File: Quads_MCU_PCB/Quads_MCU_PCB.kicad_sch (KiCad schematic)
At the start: 74 parts, among them J1 USB_C_Receptacle_USB2.0_16P, J2 Conn_01x06_Pin, J3 Conn_01x02_Pin, SW1 SW_Push, U1 STM32H723ZGTx, U2 TCAN4550RGY, U3 ISOW1044, U4 TSR_1-2450, U5 AP7361C-33E, U6 ISOW1044, U7 ISOW1044, Y1 40.000 MHz

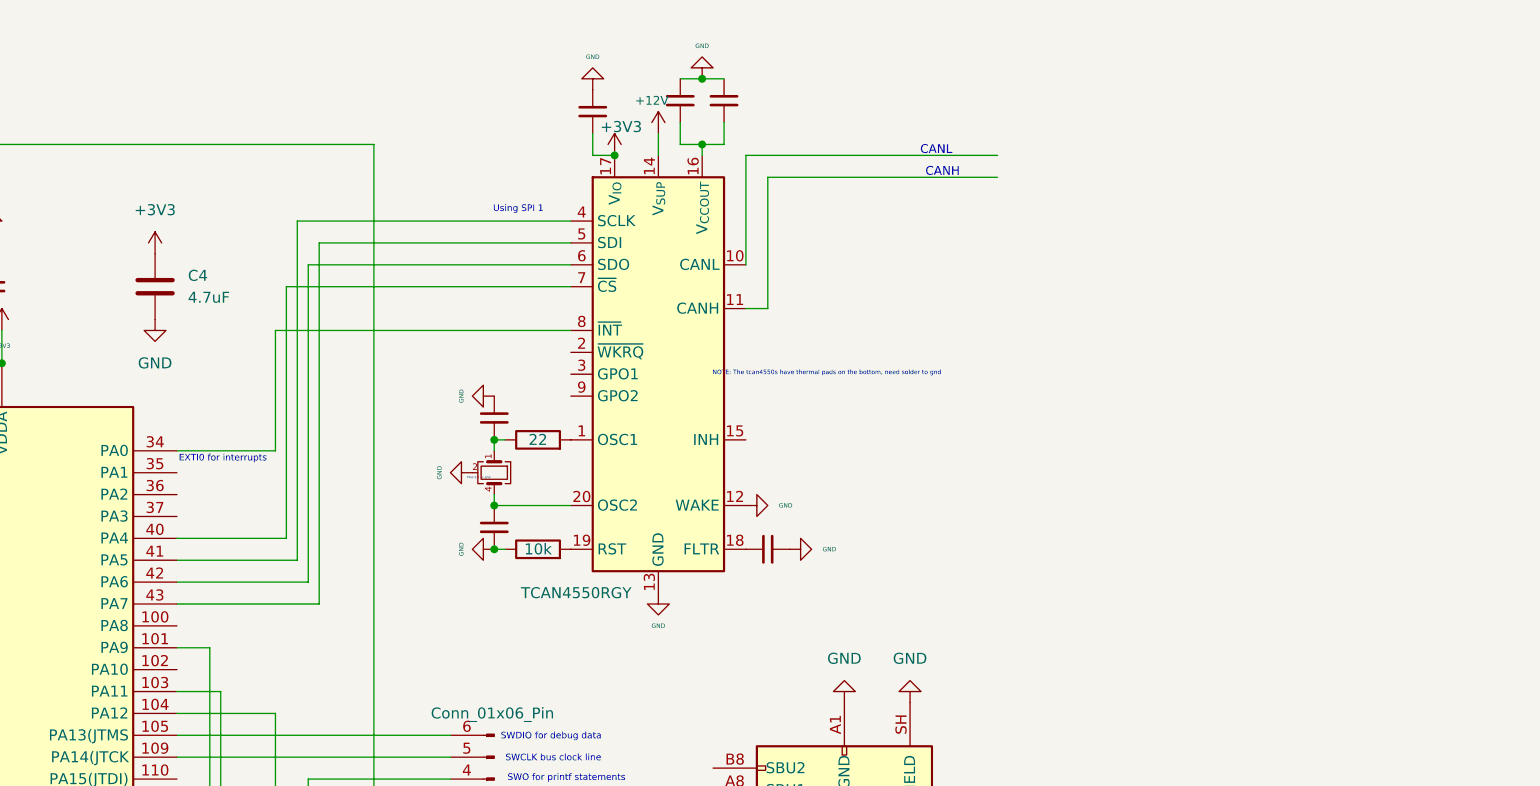
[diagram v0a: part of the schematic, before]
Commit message: Replaced tcan4550 with MCP2518FD
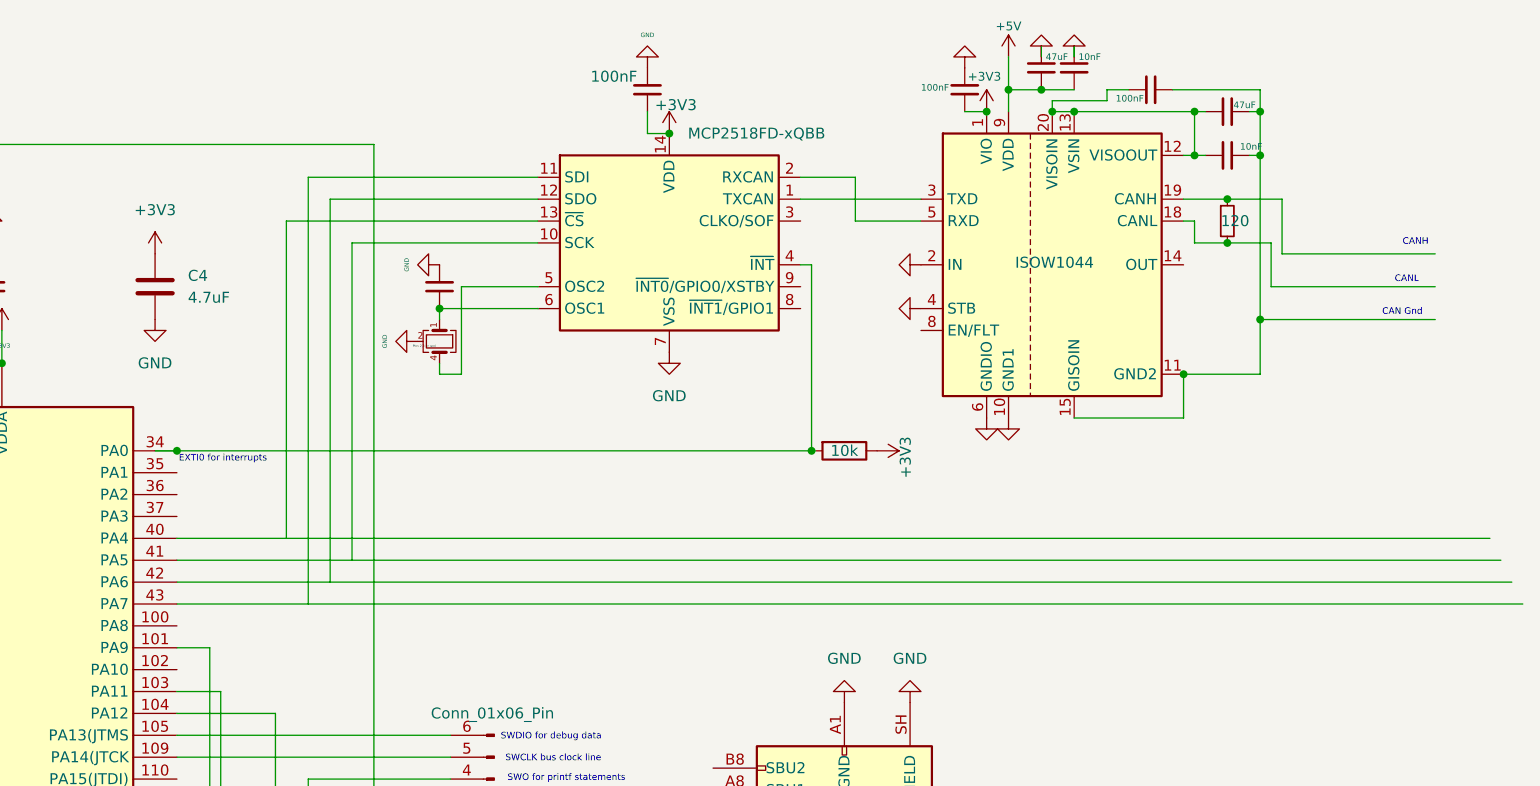
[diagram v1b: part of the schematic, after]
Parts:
- removed C21, C22: 14pF, symbol Device:C_Small
- removed C23: 100nF, symbol Device:C_Small
- removed C24, C26: 10uF, symbol Device:C_Small
- removed C25: 330nF, symbol Device:C_Small
- removed R7: 22, symbol Device:R
- removed R8: 10k, symbol Device:R
- removed U2: TCAN4550RGY, Package_DFN_QFN:Texas_RGY_R-PVQFN-N20_EP2.05x3.05mm, symbol Interface_CAN_LIN:TCAN4550RGY
- removed Y1: 40.000 MHz, symbol Device:Crystal_GND23_Small
- added C48: 14pF, symbol Device:C_Small
- added C49: 100nF, symbol Device:C_Small
- added C50, C53: 100nF, Diode_SMD:Nexperia_DSN1608-2_1.6x0.8mm, symbol Device:C_Small
- added C51, C54: 47uF, Diode_SMD:Nexperia_DSN1608-2_1.6x0.8mm, symbol Device:C_Small
- added C52, C55: 10nF, Diode_SMD:Nexperia_DSN1608-2_1.6x0.8mm, symbol Device:C_Small
- added R13: 120, Package_SO:SOIC-20W_7.5x12.8mm_P1.27mm, symbol Device:R_Small
- added R15: 10k, symbol Device:R
- added U8: MCP2518FD-xQBB, Package_DFN_QFN:DFN-14-1EP_3x4.5mm_P0.65mm_EP1.65x4.25mm, symbol Interface_CAN_LIN:MCP2518FD-xQBB
- added U9: ISOW1044, Package_SO:SOIC-20W_7.5x12.8mm_P1.27mm, symbol Interface_CAN_LIN:ISOW1044
- added Y2: 40.000 MHz, symbol Device:Crystal_GND23_Small
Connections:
- net +3V3: now also C49.2, C50.2, R15.1, U8.14 (VDD), U9.1 (VIO)
- net +5V: now also C51.2, C52.2, U9.9 (VDD)
- net GND: now also C48.2, C49.1, C50.1, C51.1, C52.1, U8.15 (VSS), U8.7 (VSS), U9.10 (GND1), U9.2 (IN), U9.4 (STB), U9.6 (GNDIO), Y2.2 (G), Y2.3 (G)
- net at U1.34 (PA0): now also R15.2, U8.4 (~{INT})
- new net: C53.1, C54.2, C55.2, U9.11 (GND2), U9.15 (GISOIN), U9.16 (GISOIN), U9.17 (GISOIN)
- new net: C53.2, C54.1, C55.1, U9.12 (VISOOUT), U9.13 (VSIN), U9.20 (VISOIN)
- new net: R13.2, U9.18 (CANL)
- new net: R13.1, U9.19 (CANH)
- new net: U8.1 (TXCAN), U9.3 (TXD)
- new net: U8.2 (RXCAN), U9.5 (RXD)
- new net: C48.1, U8.6 (OSC1), Y2.1
- new net: U8.5 (OSC2), Y2.4
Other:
- note removed: "NOTE: The tcan4550s have thermal pads on the bottom, need solder to gnd"
- note removed: "Using SPI 1"

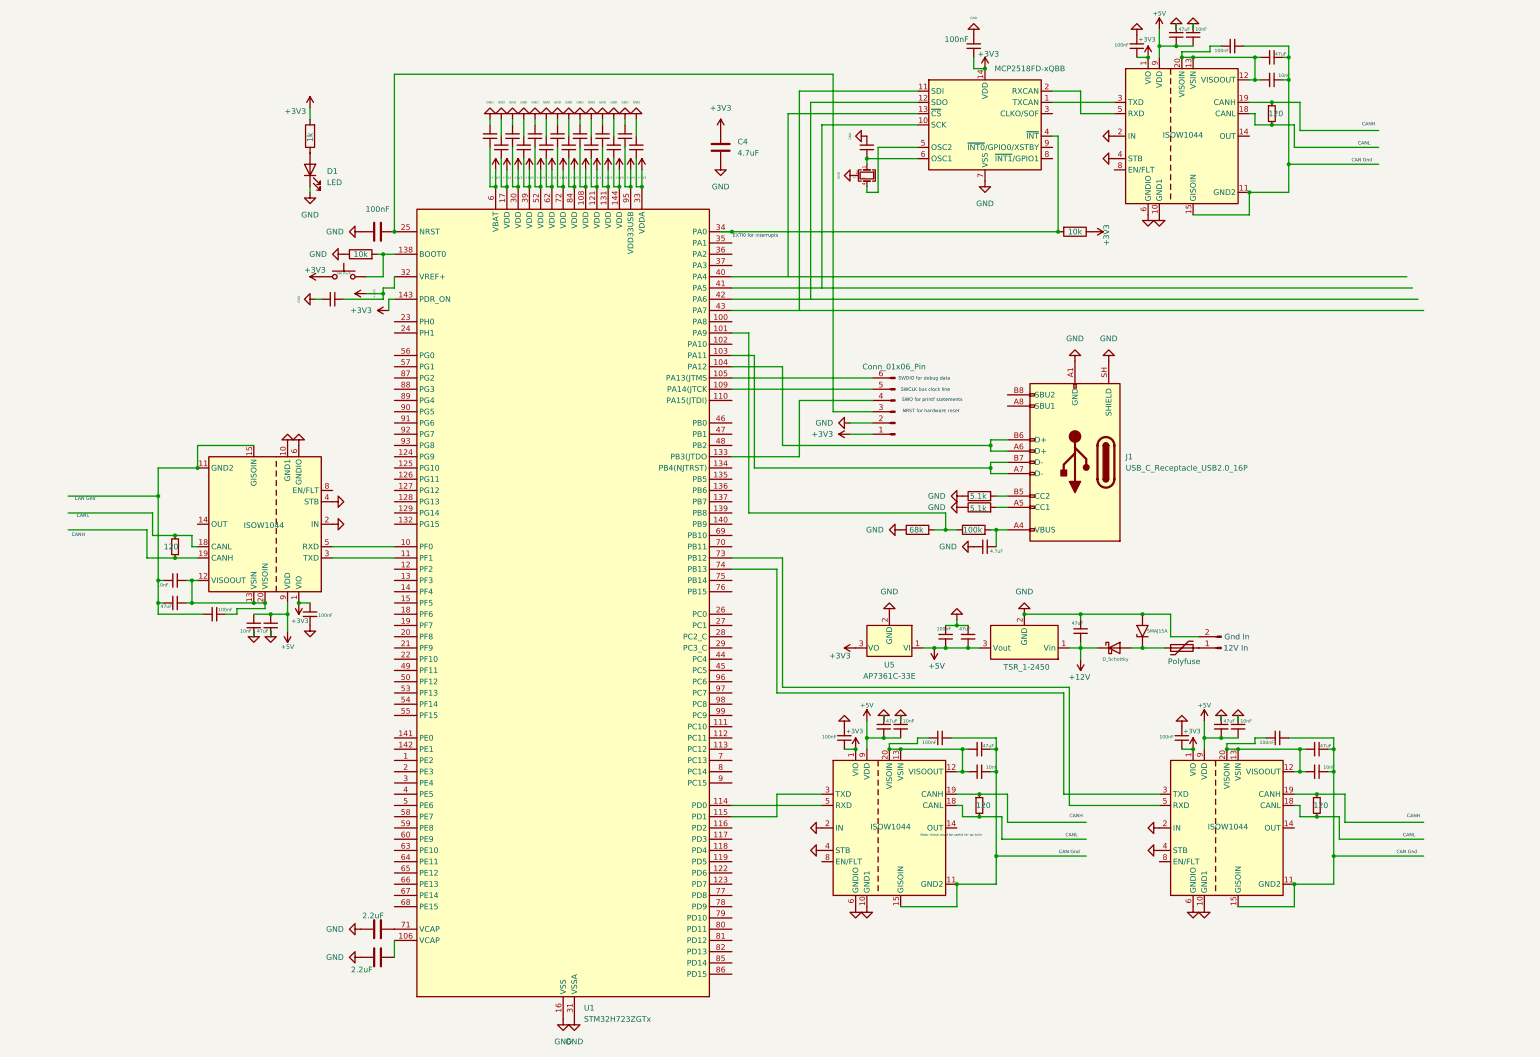
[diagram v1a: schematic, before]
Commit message: Added CAN Connectors
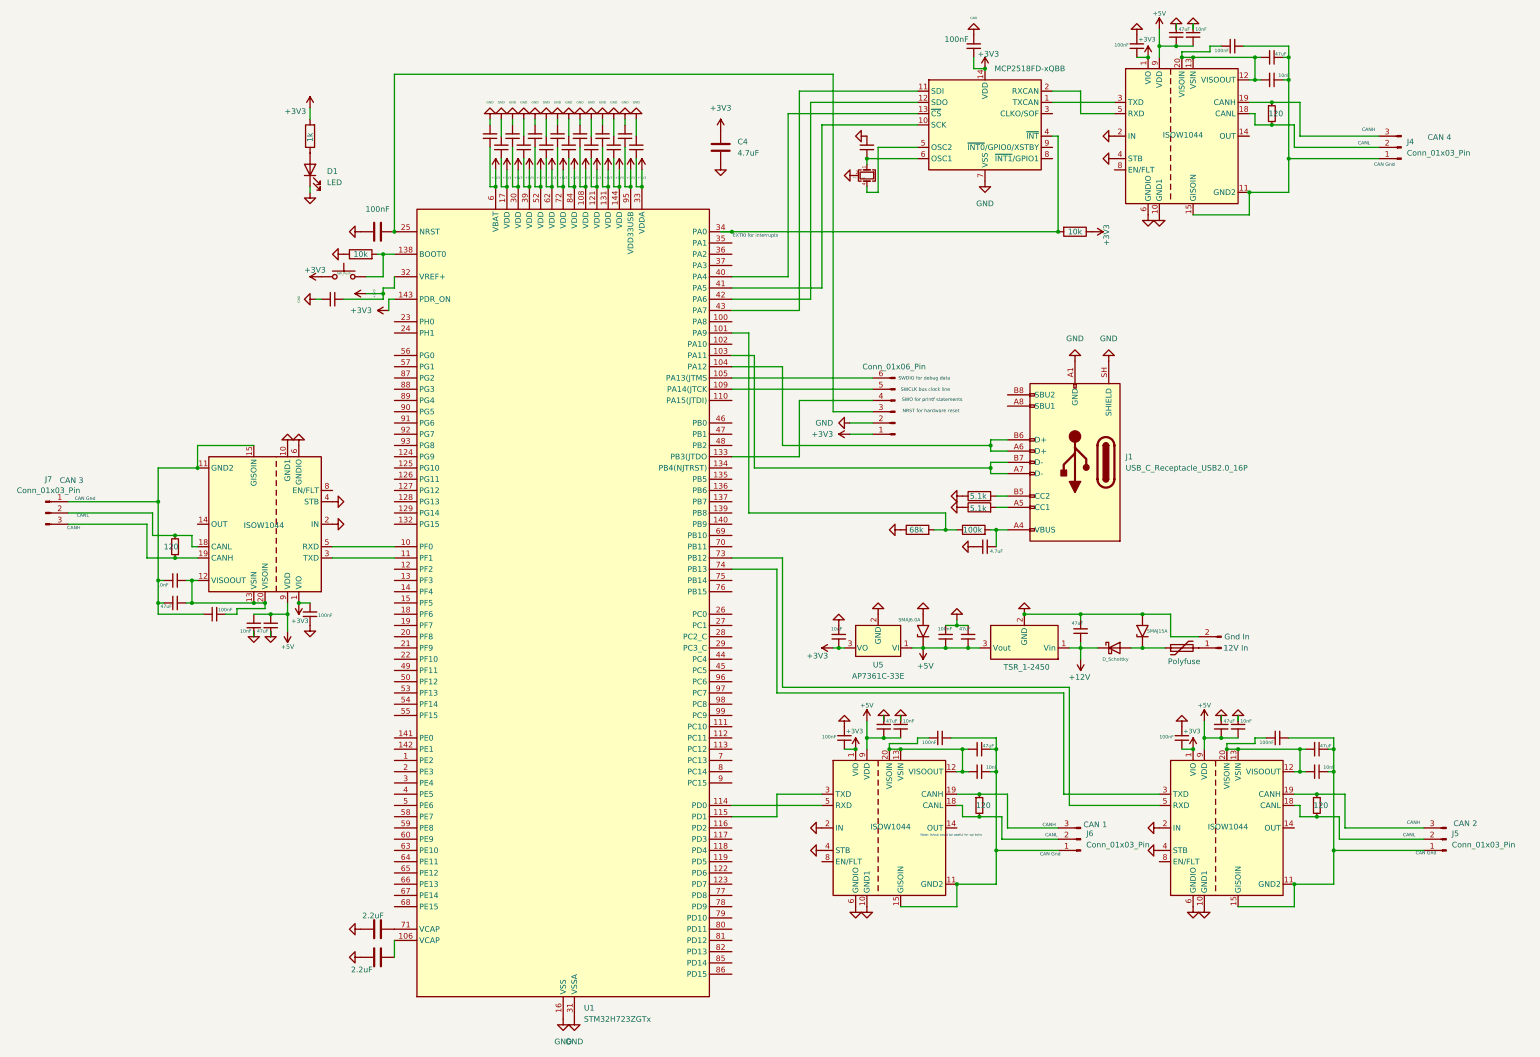
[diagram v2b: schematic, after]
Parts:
- added C56: 10uF, Diode_SMD:Nexperia_DSN1608-2_1.6x0.8mm, symbol Device:C_Small
- added D4: SMAJ6.0A, Diode_SMD:D_SMA, symbol Diode:SMAJ6.0A
- added J4, J5, J6, J7: Conn_01x03_Pin, Diode_SMD:D_SMF, symbol Connector:Conn_01x03_Pin
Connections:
- net +3V3: now also C56.2
- net +5V: now also D4.1 (A1)
- net GND: now also C56.1, D4.2 (A2)
- net at C53.1, C54.2, C55.2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: now also J4.1 (Pin_1)
- net at R13.2, U9.18 (CANL): now also J4.2 (Pin_2)
- net at R13.1, U9.19 (CANH): now also J4.3 (Pin_3)
- net at C45.1, C46.2, C47.2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: now also J7.1 (Pin_1)
- net at R11.2, U7.18 (CANL): now also J7.2 (Pin_2)
- net at R11.1, U7.19 (CANH): now also J7.3 (Pin_3)
- net at C31.2, C32.2, C35.1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: now also J6.1 (Pin_1)
- net at R9.2, U3.18 (CANL): now also J6.2 (Pin_2)
- net at R9.1, U3.19 (CANH): now also J6.3 (Pin_3)
- net at C39.1, C40.2, C41.2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: now also J5.1 (Pin_1)
- net at U1.40 (PA4): now also U8.13 (~{CS})
- net at U1.41 (PA5): now also U8.10 (SCK)
- net at U1.42 (PA6): now also U8.12 (SDO)
- net at U1.43 (PA7): now also U8.11 (SDI)
- net at R10.1, U6.19 (CANH): now also J5.3 (Pin_3)
- net at R10.2, U6.18 (CANL): now also J5.2 (Pin_2)
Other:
- note added: "CAN 1"
- note added: "CAN 2"
- note added: "CAN 3"
- note added: "CAN 4"
- moved on the sheet: U5

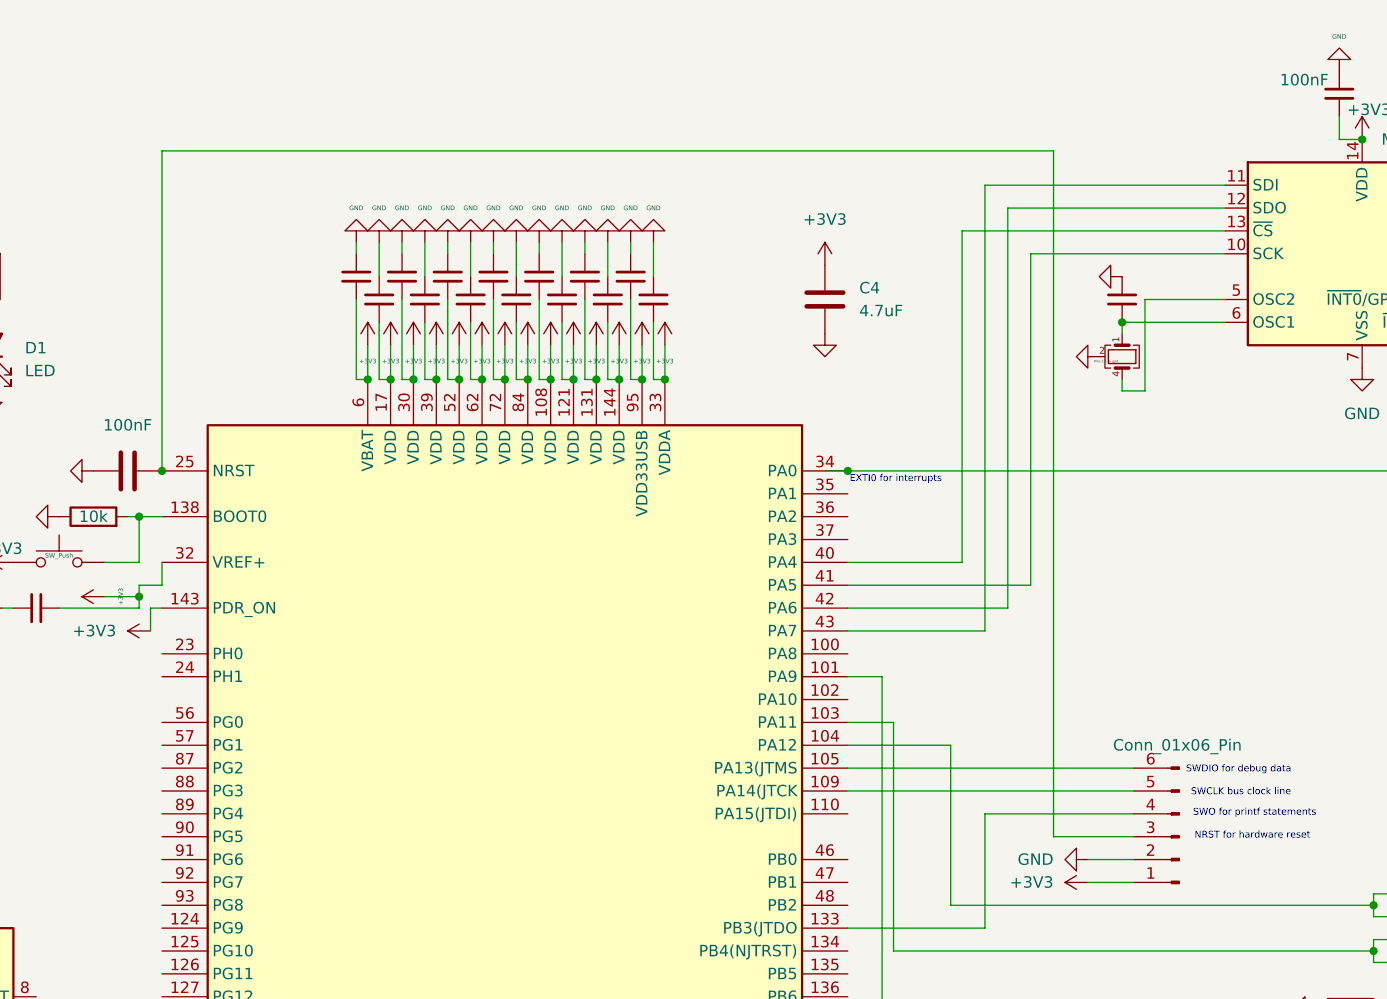
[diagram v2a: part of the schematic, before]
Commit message: Fixed the quartz clock
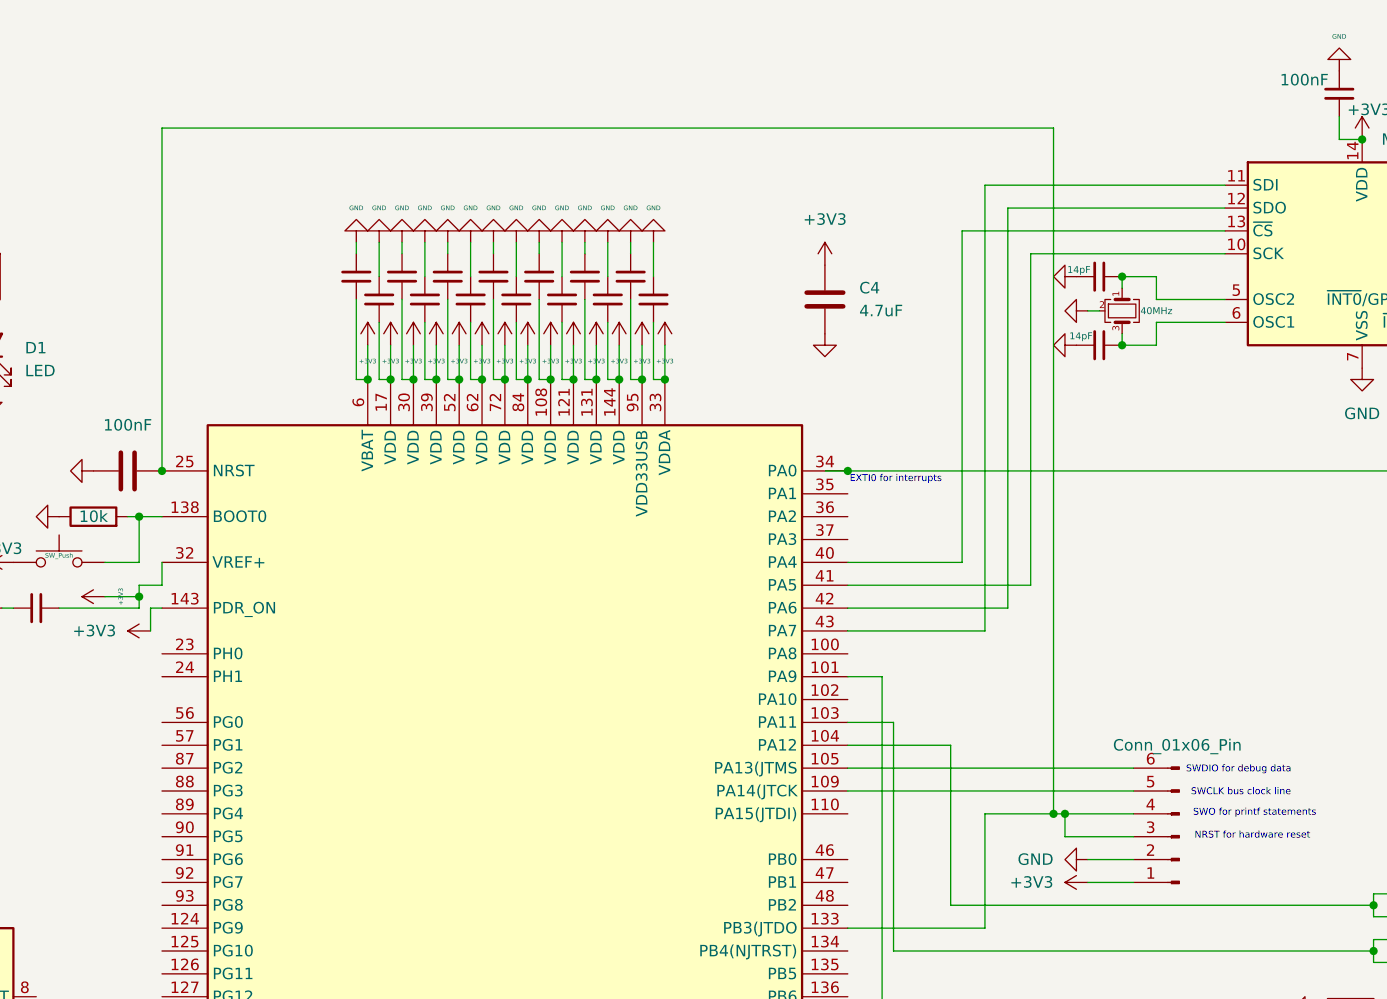
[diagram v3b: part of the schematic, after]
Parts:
- removed Y2: 40.000 MHz, symbol Device:Crystal_GND23_Small
- added C57: 14pF, symbol Device:C_Small
- added Y1: 40MHz, symbol Device:Crystal_GND24_Small
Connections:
- net GND: now also C57.2, Y1.2 (G), Y1.4 (G)
- net at C48.1: now also U8.5 (OSC2), Y1.1; no longer U8.6 (OSC1)
- net at C1.2, J2.3 (Pin_3), U1.25 (NRST): now also J2.4 (Pin_4), U1.133 (PB3(JTDO)
- new net: C57.1, U8.6 (OSC1), Y1.3
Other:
- note removed: "Pins 2,3 -> gnd"

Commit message: Fixed some wiring issues
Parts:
- C27, C28, C29, C30, C31, C32, C33, C34, C35, C36, C37, C38, C39, C40, C41, C42, C43, C44, C45, C46, C47, C50, C51, C52, C53, C54, C55, C56: footprint Diode_SMD:Nexperia_DSN1608-2_1.6x0.8mm -> (none)
- D3, D4: footprint Diode_SMD:D_SMA -> (none)
- J3: footprint Connector:Tag-Connect_TC2030-IDC-FP_2x03_P1.27mm_Vertical -> (none)
- J4, J5, J6, J7: footprint Diode_SMD:D_SMF -> (none)
- R10, R11, R13, R9: footprint Package_SO:SOIC-20W_7.5x12.8mm_P1.27mm -> (none)
- SW1: footprint Button_Switch_SMD:Nidec_Copal_CAS-120A -> Button_Switch_SMD:SW_Push_1P1T_NO_E-Switch_TL3301NxxxxxG
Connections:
- net at C1.2, J2.3 (Pin_3), U1.25 (NRST): no longer J2.4 (Pin_4), U1.133 (PB3(JTDO)
- new net: J2.4 (Pin_4), U1.133 (PB3(JTDO)
